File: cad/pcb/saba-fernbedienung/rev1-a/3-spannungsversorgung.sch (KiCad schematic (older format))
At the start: 32 parts, among them U401 TEC2-0911, U402 AP1117-18, U403 AP1117-33

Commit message: Fix: Div. DRC
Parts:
- C410, C418: value 100u -> 220u
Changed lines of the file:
@@
 P 2600 4350
 F 0 "C410" H 2718 4441 50  0000 L CNN
-F 1 "100u" H 2718 4350 50  0000 L CNN
+F 1 "220u" H 2718 4350 50  0000 L CNN
 F 2 "" H 2638 4200 50  0001 C CNN
 F 3 "~" H 2600 4350 50  0001 C CNN
@@
 P 2600 5050
 F 0 "C418" H 2718 5141 50  0000 L CNN
-F 1 "100u" H 2718 5050 50  0000 L CNN
+F 1 "220u" H 2718 5050 50  0000 L CNN
 F 2 "" H 2638 4900 50  0001 C CNN
 F 3 "~" H 2600 5050 50  0001 C CNN

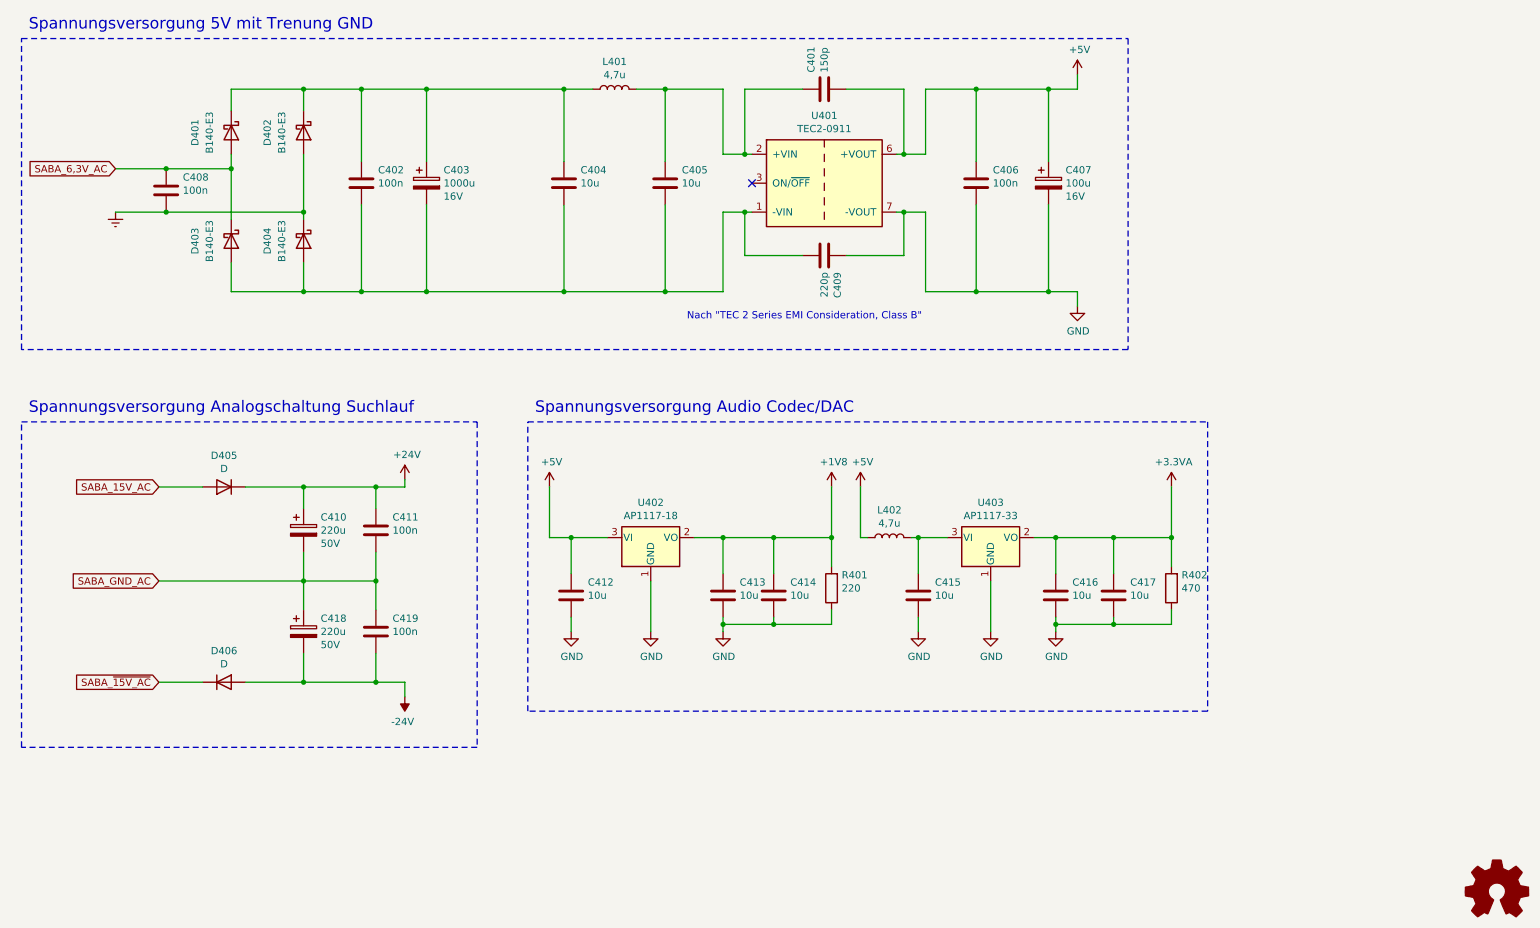
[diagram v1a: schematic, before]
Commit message: New: Bauteil - Pad Zuordnungen
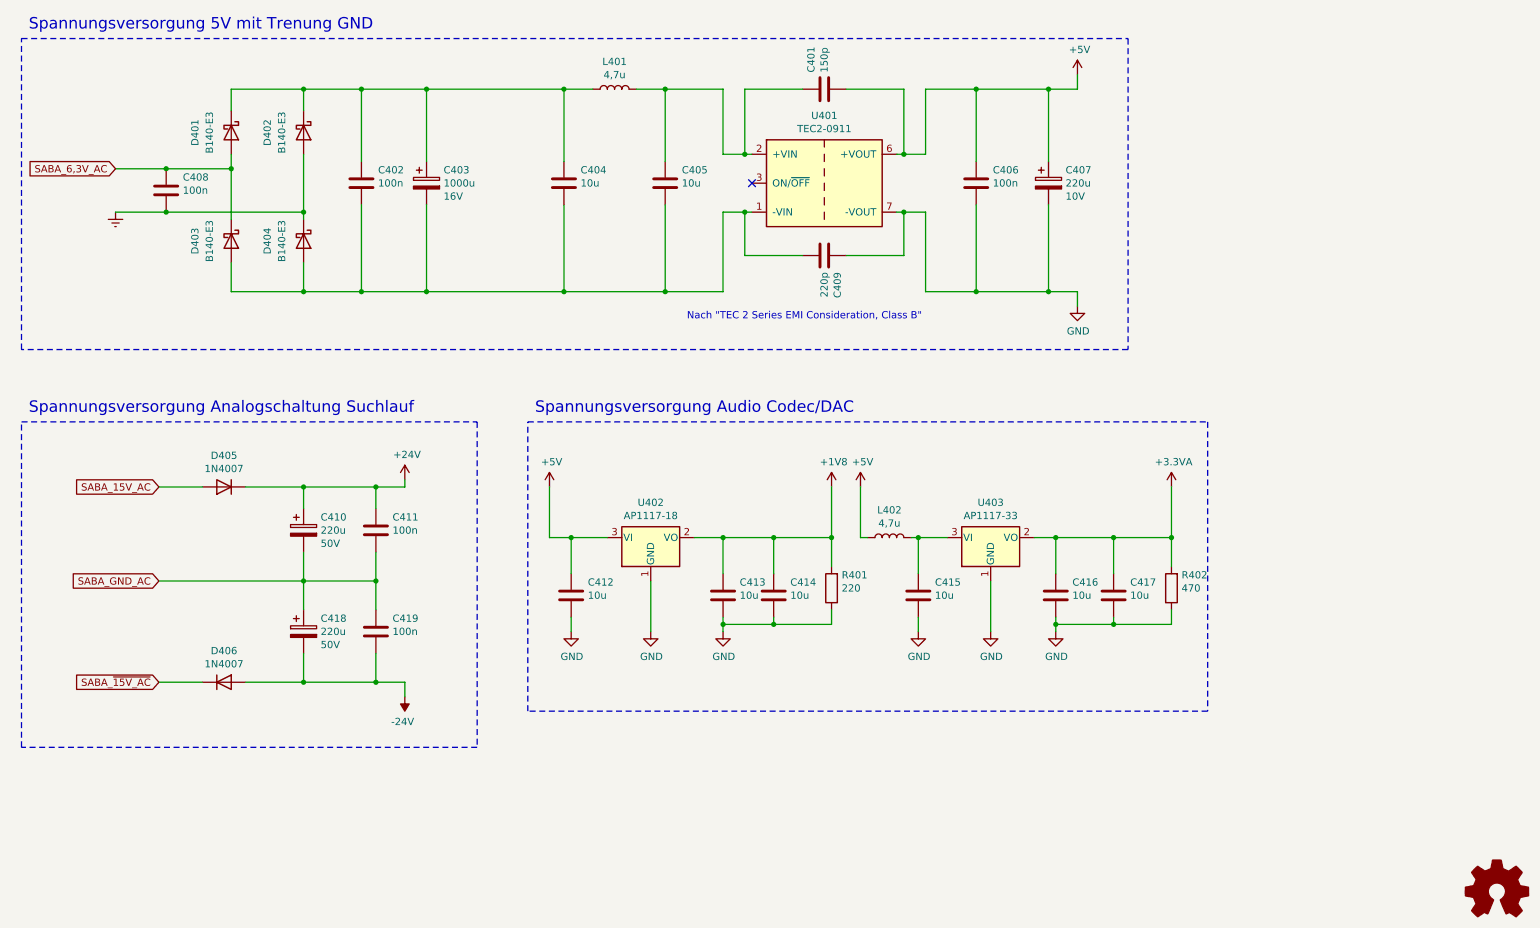
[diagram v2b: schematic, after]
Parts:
- C403, C410, C418: footprint (none) -> Capacitor_THT:CP_Radial_D10.0mm_P5.00mm
- C407: value 100u -> 220u; footprint (none) -> Capacitor_THT:CP_Radial_D10.0mm_P5.00mm; Voltage 16V -> 10V
- D405, D406: value D -> 1N4007; footprint (none) -> Diode_SMD:D_SMA
- L401, L402: footprint (none) -> local:WE-LQ; Type TDK TCK-154 -> WE 744045004
- U401: footprint (none) -> local:Converter_DCDC_TRACO_TEC2_xxxx_THT
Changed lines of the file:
@@
 F 0 "L401" V 4940 1300 50  0000 C CNN
 F 1 "4,7u" V 4849 1300 50  0000 C CNN
-F 2 "" H 4750 1300 50  0001 C CNN
+F 2 "local:WE-LQ" H 4750 1300 50  0001 C CNN
 F 3 "~" H 4750 1300 50  0001 C CNN
-F 4 "TDK TCK-154" V 4750 1300 50  0001 C CNN "Type"
+F 4 "WE 744045004" V 4750 1300 50  0001 C CNN "Type"
 	1    4750 1300
 	0    -1   -1   0
@@
 F 0 "U401" H 6200 2417 50  0000 C CNN
 F 1 "TEC2-0911" H 6200 2326 50  0000 C CNN
-F 2 "" H 6200 1950 50  0001 C CNN
+F 2 "local:Converter_DCDC_TRACO_TEC2_xxxx_THT" H 6200 1950 50  0001 C CNN
 F 3 "" H 6200 1950 50  0001 C CNN
 	1    6200 1950
@@
 P 7750 1950
 F 0 "C407" H 7868 2041 50  0000 L CNN
-F 1 "100u" H 7868 1950 50  0000 L CNN
-F 2 "" H 7788 1800 50  0001 C CNN
+F 1 "220u" H 7868 1950 50  0000 L CNN
+F 2 "Capacitor_THT:CP_Radial_D10.0mm_P5.00mm" H 7788 1800 50  0001 C CNN
 F 3 "~" H 7750 1950 50  0001 C CNN
-F 4 "16V" H 7868 1859 50  0000 L CNN "Voltage"
+F 4 "10V" H 7868 1859 50  0000 L CNN "Voltage"
 	1    7750 1950
 	1    0    0    -1
@@
 F 0 "C403" H 3568 2041 50  0000 L CNN
 F 1 "1000u" H 3568 1950 50  0000 L CNN
-F 2 "" H 3488 1800 50  0001 C CNN
+F 2 "Capacitor_THT:CP_Radial_D10.0mm_P5.00mm" H 3488 1800 50  0001 C CNN
 F 3 "~" H 3450 1950 50  0001 C CNN
 F 4 "16V" H 3568 1859 50  0000 L CNN "Voltage"
@@
 P 2050 4050
 F 0 "D405" H 2050 3833 50  0000 C CNN
-F 1 "D" H 2050 3924 50  0000 C CNN
-F 2 "" H 2050 4050 50  0001 C CNN
+F 1 "1N4007" H 2050 3924 50  0000 C CNN
+F 2 "Diode_SMD:D_SMA" H 2050 4050 50  0001 C CNN
 F 3 "~" H 2050 4050 50  0001 C CNN
 	1    2050 4050
@@
 P 2050 5400
 F 0 "D406" H 2050 5617 50  0000 C CNN
-F 1 "D" H 2050 5526 50  0000 C CNN
-F 2 "" H 2050 5400 50  0001 C CNN
+F 1 "1N4007" H 2050 5526 50  0000 C CNN
+F 2 "Diode_SMD:D_SMA" H 2050 5400 50  0001 C CNN
 F 3 "~" H 2050 5400 50  0001 C CNN
 	1    2050 5400
@@
 F 0 "C410" H 2718 4441 50  0000 L CNN
 F 1 "220u" H 2718 4350 50  0000 L CNN
-F 2 "" H 2638 4200 50  0001 C CNN
+F 2 "Capacitor_THT:CP_Radial_D10.0mm_P5.00mm" H 2638 4200 50  0001 C CNN
 F 3 "~" H 2600 4350 50  0001 C CNN
 F 4 "50V" H 2718 4259 50  0000 L CNN "Voltage"
@@
 F 0 "C418" H 2718 5141 50  0000 L CNN
 F 1 "220u" H 2718 5050 50  0000 L CNN
-F 2 "" H 2638 4900 50  0001 C CNN
+F 2 "Capacitor_THT:CP_Radial_D10.0mm_P5.00mm" H 2638 4900 50  0001 C CNN
 F 3 "~" H 2600 5050 50  0001 C CNN
 F 4 "50V" H 2718 4959 50  0000 L CNN "Voltage"
@@
 F 0 "L402" V 6840 4400 50  0000 C CNN
 F 1 "4,7u" V 6749 4400 50  0000 C CNN
-F 2 "" H 6650 4400 50  0001 C CNN
+F 2 "local:WE-LQ" H 6650 4400 50  0001 C CNN
 F 3 "~" H 6650 4400 50  0001 C CNN
-F 4 "TDK TCK-154" V 6650 4400 50  0001 C CNN "Type"
+F 4 "WE 744045004" V 6650 4400 50  0001 C CNN "Type"
 	1    6650 4400
 	0    -1   -1   0

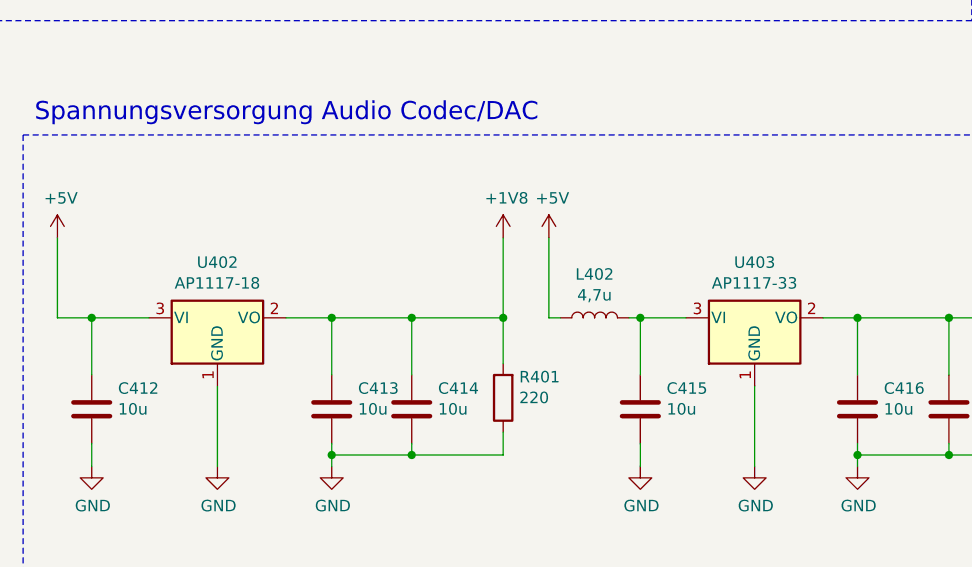
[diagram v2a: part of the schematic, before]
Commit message: Add: Bauteiltypen Digikey...
viele Bauteile von WE da hoffentlich lange gueltig...
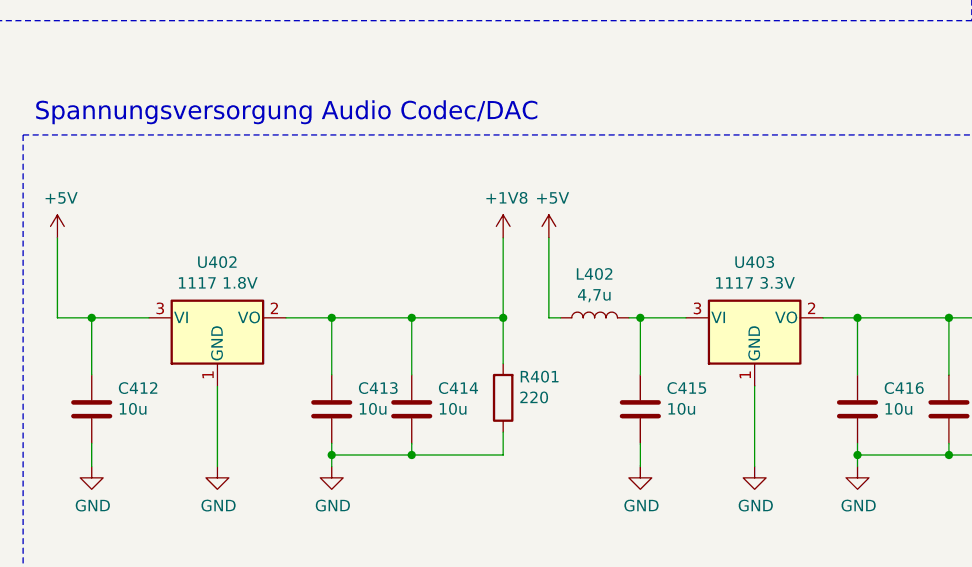
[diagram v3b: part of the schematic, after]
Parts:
- C401: Bauteil (none) -> 885012206103
- C402, C406, C408, C411, C419: Bauteil (none) -> WE 885382206004
- C403: Bauteil (none) -> WE 860020375017
- C404, C405, C412, C413, C414, C415, C416, C417: Bauteil (none) -> WE 885012208069
- C407, C410, C418: Bauteil (none) -> WE 860020675020
- C409: Bauteil (none) -> WE 885012206079
- D401, D402, D403, D404: Bauteil (none) -> Vishay B140-E3/61T
- D405, D406: Bauteil (none) -> 1N4007FLTR
- L401, L402: Bauteil (none) -> WE 744045004; Type WE 744045004 -> (none)
- U401: Bauteil (none) -> Traco Power TEC 2-0911
- U402: value AP1117-18 -> 1117 1.8V; Bauteil (none) -> ST LD1117S18CTR
- U403: value AP1117-33 -> 1117 3.3V; Bauteil (none) -> ST LD1117S33CTR

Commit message: Change: Relais SMT -> THT, Sicherung PCB
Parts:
- C401: Bauteil 885012206103 -> WE 885012206103
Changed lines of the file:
@@
 encoding utf-8
 Sheet 4 7
-Title "Fernbedienung SABA 6-3D"
-Date "2021-01-13"
+Title "Fernbedienung - Webradio SABA 6-3D"
+Date "2021-01-14"
 Rev "1-A"
 Comp "Martin Wagner DL2WAG"
@@
 Comment2 ""
 Comment3 "(Meersburg/Freiburg 6-3D, weitere?)"
-Comment4 "Fernbedienung für SABA \"Automatic\" Radios"
+Comment4 "Fernbedienung - Webradio für SABA \"Automatic\" Radios"
 $EndDescr
 $Comp
@@
 F 3 "~" H 6200 1300 50  0001 C CNN
 F 4 "" H 6315 1209 50  0000 L CNN "Placement"
-F 5 "885012206103" H 6200 1300 50  0001 C CNN "Bauteil"
+F 5 "WE 885012206103" H 6200 1300 50  0001 C CNN "Bauteil"
 	1    6200 1300
 	0    -1   -1   0

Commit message: Fab Layer
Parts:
- C407: footprint Capacitor_THT:CP_Radial_D10.0mm_P5.00mm -> local:CP_Radial_D10.0mm_P5.00mm_liegend
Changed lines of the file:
@@
 F 0 "C407" H 7868 2041 50  0000 L CNN
 F 1 "220u" H 7868 1950 50  0000 L CNN
-F 2 "Capacitor_THT:CP_Radial_D10.0mm_P5.00mm" H 7788 1800 50  0001 C CNN
+F 2 "local:CP_Radial_D10.0mm_P5.00mm_liegend" H 7788 1800 50  0001 C CNN
 F 3 "~" H 7750 1950 50  0001 C CNN
 F 4 "10V" H 7868 1859 50  0000 L CNN "Voltage"

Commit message: Fix: Opamp zweifach
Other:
- note added: "Spannungsversorgung 5V mit Trennung GND"
- note removed: "Spannungsversorgung 5V mit Trenung GND"
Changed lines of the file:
@@
 	3450 2700 4400 2700
 Text Notes 700  900  0    79   ~ 0
-Spannungsversorgung 5V mit Trenung GND
+Spannungsversorgung 5V mit Trennung GND
 Wire Notes Line
 	650  950  8300 950
